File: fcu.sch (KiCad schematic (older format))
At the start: 38 parts

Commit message: Update components
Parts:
- removed Q?: TP0610L, TO_SOT_Packages_THT:TO-92_Molded_Narrow, symbol TP0610L
- added C? (x2): 100n, symbol C
- added D?: D, symbol D
- added Q?: IRLIZ44N, TO_SOT_Packages_THT:TO-220_Vertical, symbol IRLIZ44N
- added R? (x2): 10K, symbol R
- added R?: 1K, symbol R
- J?: value Conn_01x02 -> UART Connector; footprint (none) -> Connectors_JST:JST_GH_BM02B-GHS-TBT_02x1.25mm_Straight
- J?: value Conn_01x05 -> JST Connector; footprint (none) -> Connectors_JST:JST_GH_BM05B-GHS-TBT_05x1.25mm_Straight
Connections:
- net VCC5 is gone; now on net SOLENOID_P: U?.2 (VO), U?.3 (VI)
- net GND: now also C?.2, C?.2, Q?.3 (S); no longer J?.5 (Pin_5)
- net IOVDD: now also R?.1, R?.1
- net SOLENOID_EN: now also R?.2
- net SOLENOID_PWR renamed SOLENOID_P
- net SOLENOID_P: now also D?.1 (K)
- net TRIGGER_CONTACT renamed TRIGGER_SWITCH
- net TRIGGER_SWITCH: now also C?.1, R?.2
- net TRIGGER_NEUTRAL renamed SELECTOR_SWITCH
- net SELECTOR_SWITCH: now also C?.1, R?.2
- new net: Q?.1 (G), R?.1
- new net SOLENOID_N: D?.2 (A), J?.5 (Pin_5), Q?.2 (D)
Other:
- note added: "Debug UART port\n"
- note added: "Main\n"
- note added: "Solenoid Control Circuit"
- note added: "Trigger Board Connection"
- note added: "Wolverine Custom Bluetooth FCU"
- moved on the sheet: J?

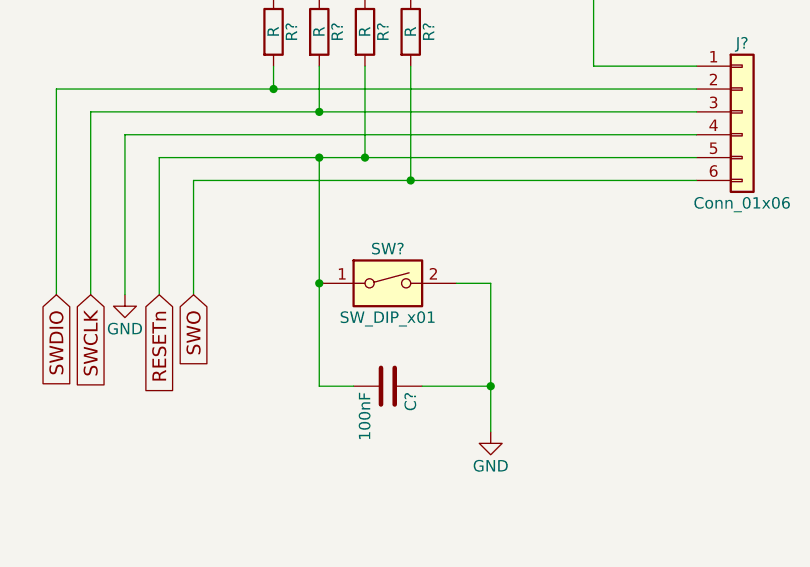
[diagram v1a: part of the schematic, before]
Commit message: replace dip switch with push button
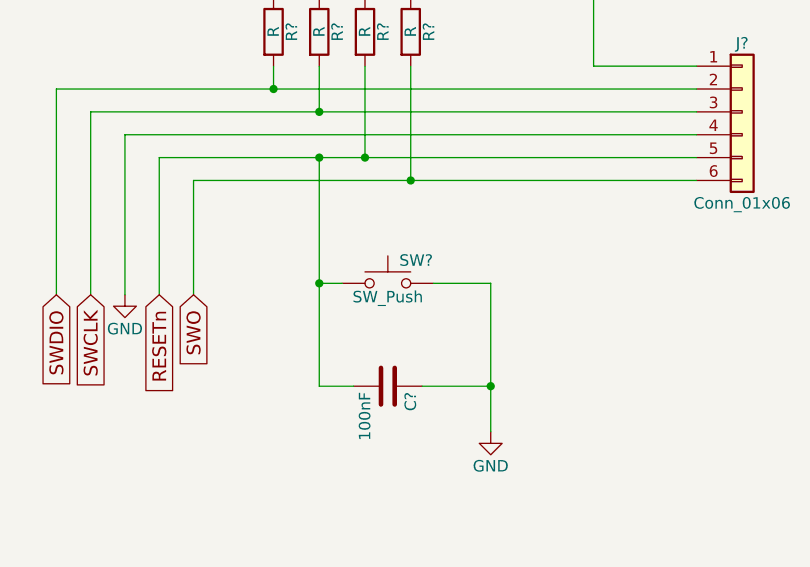
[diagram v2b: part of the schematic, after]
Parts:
- removed SW?: SW_DIP_x01, symbol SW_DIP_x01
- added SW?: SW_Push, symbol SW_Push
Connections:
- net GND: now also SW?.2
- net RESETn: now also SW?.1
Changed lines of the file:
@@
 Wire Wire Line
 	13100 3950 13100 4000
-$Comp
-L SW_DIP_x01 SW?
-U 1 1 5A14BD3F
-P 13600 5250
-F 0 "SW?" H 13600 5400 50  0000 C CNN
-F 1 "SW_DIP_x01" H 13600 5100 50  0000 C CNN
-F 2 "" H 13600 5250 50  0001 C CNN
-F 3 "" H 13600 5250 50  0001 C CNN
-	1    13600 5250
-	1    0    0    -1
-$EndComp
 Wire Wire Line
 	13300 4700 13300 5700
@@
 Wire Wire Line
 	13300 5700 13450 5700
-Connection ~ 13300 5250
-Wire Wire Line
-	13900 5250 14050 5250
+Wire Wire Line
+	13800 5250 14050 5250
 Wire Wire Line
 	14050 5250 14050 5900
@@
 Text Notes 1350 5700 0    59   ~ 0
 Solenoid Control Circuit
+$Comp
+L SW_Push SW?
+U 1 1 5A15DBA5
+P 13600 5250
+F 0 "SW?" H 13650 5350 50  0000 L CNN
+F 1 "SW_Push" H 13600 5190 50  0000 C CNN
+F 2 "" H 13600 5450 50  0001 C CNN
+F 3 "" H 13600 5450 50  0001 C CNN
+	1    13600 5250
+	1    0    0    -1
+$EndComp
+Wire Wire Line
+	13300 5250 13400 5250
+Connection ~ 13300 5250
 $EndSCHEMATC

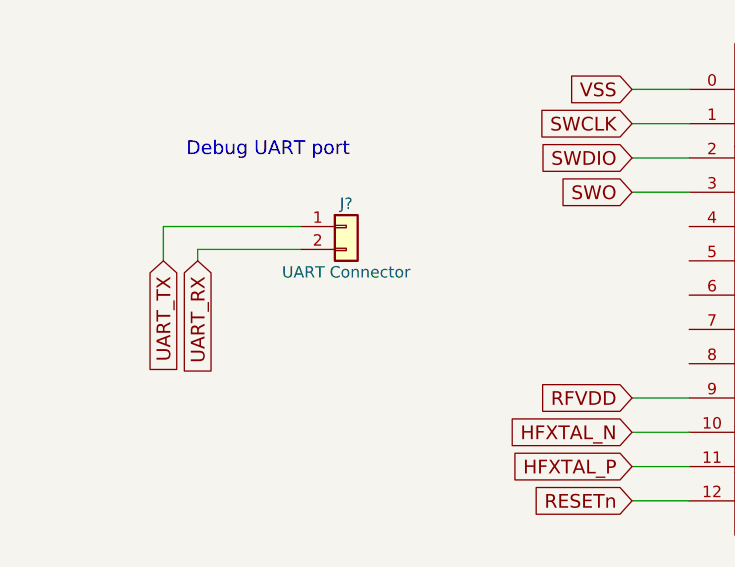
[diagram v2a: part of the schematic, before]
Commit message: Add ground for 3pin UART connector
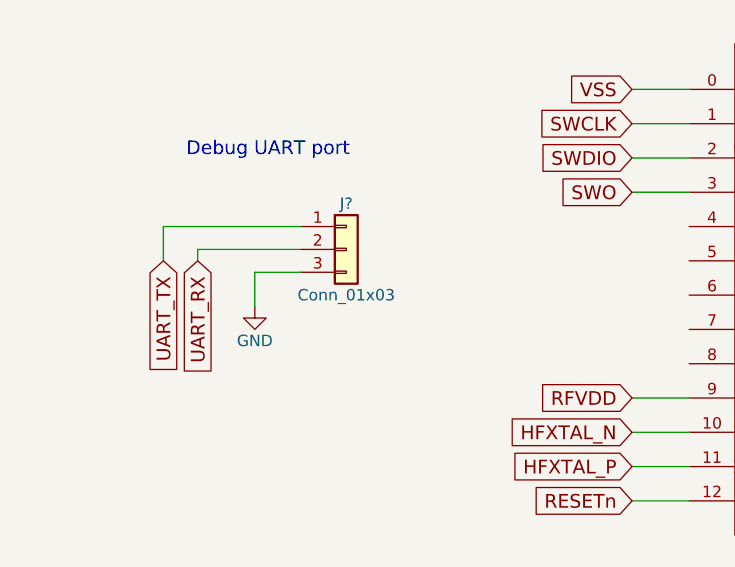
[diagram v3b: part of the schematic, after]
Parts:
- removed J?: UART Connector, Connectors_JST:JST_GH_BM02B-GHS-TBT_02x1.25mm_Straight, symbol Conn_01x02
- added J?: Conn_01x03, Connectors_JST:JST_GH_BM05B-GHS-TBT_05x1.25mm_Straight, symbol Conn_01x03
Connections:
- net GND: now also J?.3 (Pin_3)
- net UART_RX: now also J?.2 (Pin_2)
- net UART_TX: now also J?.1 (Pin_1)
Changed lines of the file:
@@
 Wire Wire Line
 	13150 8850 13150 9100
-$Comp
-L Conn_01x02 J?
-U 1 1 5A14E979
-P 2050 3300
-F 0 "J?" H 2050 3400 50  0000 C CNN
-F 1 "UART Connector" H 2050 3100 50  0000 C CNN
-F 2 "Connectors_JST:JST_GH_BM02B-GHS-TBT_02x1.25mm_Straight" H 2050 3300 50  0001 C CNN
-F 3 "" H 2050 3300 50  0001 C CNN
-	1    2050 3300
-	1    0    0    -1
-$EndComp
 Text GLabel 1250 3450 3    60   Input ~ 0
 UART_TX
@@
 	13300 5250 13400 5250
 Connection ~ 13300 5250
+$Comp
+L Conn_01x03 J?
+U 1 1 5A15EE28
+P 2050 3400
+F 0 "J?" H 2050 3600 50  0000 C CNN
+F 1 "Conn_01x03" H 2050 3200 50  0000 C CNN
+F 2 "Connectors_JST:JST_GH_BM05B-GHS-TBT_05x1.25mm_Straight" H 2050 3400 50  0001 C CNN
+F 3 "" H 2050 3400 50  0001 C CNN
+	1    2050 3400
+	1    0    0    -1
+$EndComp
+$Comp
+L GND #PWR?
+U 1 1 5A15EEAB
+P 1650 3650
+F 0 "#PWR?" H 1650 3400 50  0001 C CNN
+F 1 "GND" H 1650 3500 50  0000 C CNN
+F 2 "" H 1650 3650 50  0001 C CNN
+F 3 "" H 1650 3650 50  0001 C CNN
+	1    1650 3650
+	1    0    0    -1
+$EndComp
+Wire Wire Line
+	1650 3650 1650 3500
+Wire Wire Line
+	1650 3500 1850 3500
 $EndSCHEMATC
